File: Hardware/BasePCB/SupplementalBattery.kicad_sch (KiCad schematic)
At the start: 28 parts, among them J1 53307-2471, Q6 IRLML0030

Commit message: only 4 traces left
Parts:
- added J10: 575-4, UTSVT_Connectors:5754, symbol Connector_Generic:Conn_01x01
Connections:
- net SUPP_REG+: now also J10.1 (Pin_1)
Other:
- note added: "24V injector"
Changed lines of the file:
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@@
 		)
 	)
+	(text "24V injector"
+		(exclude_from_sim no)
+		(at 202.184 33.274 0)
+		(effects
+			(font
+				(size 1.27 1.27)
+			)
+		)
+	)
 	(text "Connector to SuppMon Hat"
 		(exclude_from_sim no)
@@
 	)
 	(junction
+		(at 201.93 43.18)
+		(diameter 0)
+		(color 0 0 0 0)
+	)
+	(junction
 		(at 189.23 43.18)
 		(diameter 0)
@@
 	(wire
 		(pts
+			(xy 196.85 34.29) (xy 201.93 34.29)
+		)
+		(stroke
+			(width 0)
+			(type default)
+		)
+	)
+	(wire
+		(pts
 			(xy 34.29 68.58) (xy 34.29 69.85)
 		)
@@
 	(wire
 		(pts
-			(xy 189.23 43.18) (xy 203.2 43.18)
+			(xy 189.23 43.18) (xy 201.93 43.18)
 		)
 		(stroke
@@
 	(wire
 		(pts
+			(xy 201.93 34.29) (xy 201.93 43.18)
+		)
+		(stroke
+			(width 0)
+			(type default)
+		)
+	)
+	(wire
+		(pts
 			(xy 40.64 43.18) (xy 49.53 43.18)
 		)
@@
 	(wire
 		(pts
+			(xy 201.93 43.18) (xy 203.2 43.18)
+		)
+		(stroke
+			(width 0)
+			(type default)
+		)
+	)
+	(wire
+		(pts
 			(xy 83.82 137.16) (xy 88.9 137.16)
 		)
@@
 	)
 	(symbol
+		(lib_id "Connector_Generic:Conn_01x01")
+		(at 191.77 34.29 0)
+		(mirror y)
+		(unit 1)
+		(exclude_from_sim no)
+		(in_bom yes)
+		(on_board yes)
+		(dnp no)
+		(fields_autoplaced yes)
+		(property "Reference" "J10"
+			(at 191.77 27.94 0)
+			(effects
+				(font
+					(size 1.27 1.27)
+				)
+			)
+		)
+		(property "Value" "575-4"
+			(at 191.77 30.48 0)
+			(effects
+				(font
+					(size 1.27 1.27)
+				)
+			)
+		)
+		(property "Footprint" "UTSVT_Connectors:5754"
+			(at 191.77 34.29 0)
+			(effects
+				(font
+					(size 1.27 1.27)
+				)
+				(hide yes)
+			)
+		)
+		(property "Datasheet" "~"
+			(at 191.77 34.29 0)
+			(effects
+				(font
+					(size 1.27 1.27)
+				)
+				(hide yes)
+			)
+		)
+		(property "Description" "Generic connector, single row, 01x01, script generated (kicad-library-utils/schlib/autogen/connector/)"
+			(at 191.77 34.29 0)
+			(effects
+				(font
+					(size 1.27 1.27)
+				)
+				(hide yes)
+			)
+		)
+		(property "P/N" "575-4"
+			(at 191.77 34.29 0)
+			(effects
+				(font
+					(size 1.27 1.27)
+				)
+				(hide yes)
+			)
+		)
+		(property "Mouser P/N" "534-575-4"
+			(at 191.77 34.29 0)
+			(effects
+				(font
+					(size 1.27 1.27)
+				)
+				(hide yes)
+			)
+		)
+		(property "Digikey P/N" "36-575-4-ND"
+			(at 191.77 34.29 0)
+			(effects
+				(font
+					(size 1.27 1.27)
+				)
+				(hide yes)
+			)
+		)
+		(pin "1"
+		)
+		(instances
+			(project "LV Carrier Board"
+				(path "/c5c5922b-1600-4b67-acf3-33264cecd75b/d4cbd764-e723-45ee-b4b7-e620455af31e"
+					(reference "J10")
+					(unit 1)
+				)
+			)
+		)
+	)
+	(symbol
 		(lib_id "Connector:TestPoint")
 		(at 189.23 43.18 0)
@@
 			)
 		)
-		(pin "INP" input
+		(pin "INP" bidirectional
 			(at 107.95 43.18 180)
 			(effects
@@
 			)
 		)
-		(pin "INN" output
+		(pin "INN" bidirectional
 			(at 132.08 43.18 0)
 			(effects

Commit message: add JLC p/n
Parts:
- D14, D15, D16: Assemble (none) -> Y; LSCC P/N (none) -> C7371904
- J1: Assemble (none) -> N; Mouser Price/Stock https://www.mouser.co.uk/ProductDetail/Molex/53307-2471?qs=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 -> (none)
- J10, TP1, TP11, TP12, TP19, TP2, TP21, TP28, TP3, TP7, TP8: Assemble (none) -> N
- Q6: Assemble (none) -> Y; LSCC P/N (none) -> C67272; P/N (none) -> IRLML0030
- R1: Assemble (none) -> Y; LSCC P/N (none) -> C23354
- R14, R15: Assemble (none) -> N; LSCC P/N (none) -> C25804
- R27, R28, R29: Assemble (none) -> Y; LSCC P/N (none) -> C23162
- R30, R34: Assemble (none) -> N; LSCC P/N (none) -> C21189
- R33: Assemble (none) -> Y; LSCC P/N (none) -> C25803; P/N CRCW06034K30FKTA -> CRCW0603100KFKEE
- R41: Assemble (none) -> Y; LSCC P/N (none) -> C21190
- R44: Assemble (none) -> Y; LSCC P/N (none) -> C25804
- U4: Assemble (none) -> N; Datasheet2 https://www.vicorpower.com/documents/datasheets/ds_24vin-mi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 -> (none)

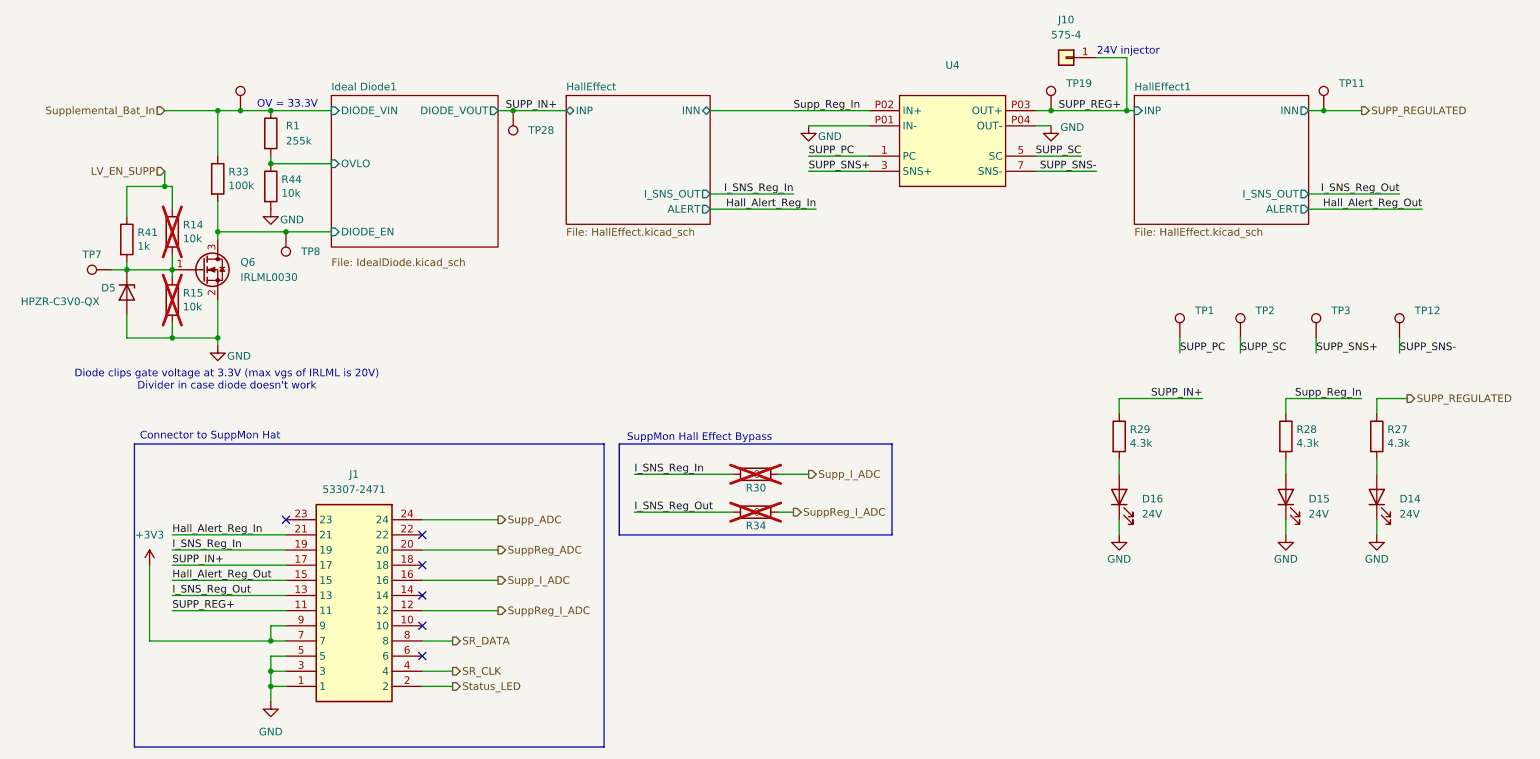
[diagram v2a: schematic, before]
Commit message: new hall effect IC
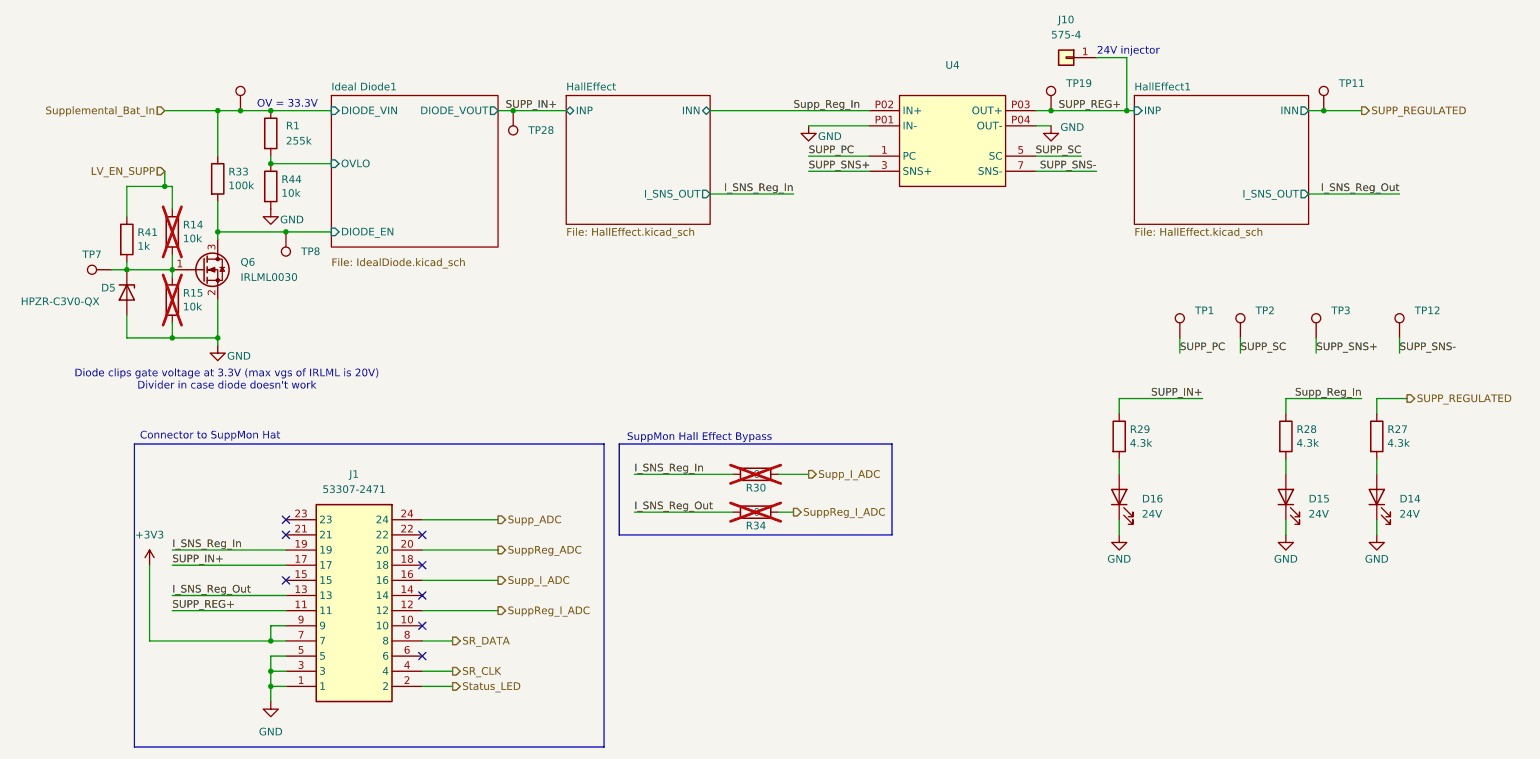
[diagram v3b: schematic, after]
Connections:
- net Hall_Alert_Reg_In: no longer names the net of J1.21
- net Hall_Alert_Reg_Out: no longer names the net of J1.15
- no-connect marks 6 -> 8
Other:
- sheet HallEffect ports: added none; removed ALERT
- sheet HallEffect1 ports: added none; removed ALERT
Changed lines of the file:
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@@
 		(at 60.96 111.76)
 	)
+	(no_connect
+		(at 60.96 114.3)
+	)
+	(no_connect
+		(at 60.96 121.92)
+	)
 	(wire
 		(pts
@@
 	(wire
 		(pts
-			(xy 41.91 121.92) (xy 60.96 121.92)
-		)
-		(stroke
-			(width 0)
-			(type default)
-		)
-	)
-	(wire
-		(pts
 			(xy 31.75 69.85) (xy 34.29 69.85)
 		)
@@
 	(wire
 		(pts
-			(xy 132.08 59.69) (xy 149.86 59.69)
-		)
-		(stroke
-			(width 0)
-			(type default)
-		)
-	)
-	(wire
-		(pts
 			(xy 58.42 129.54) (xy 58.42 132.08)
 		)
@@
 	(wire
 		(pts
-			(xy 41.91 114.3) (xy 60.96 114.3)
-		)
-		(stroke
-			(width 0)
-			(type default)
-		)
-	)
-	(wire
-		(pts
 			(xy 243.84 91.44) (xy 248.92 91.44)
 		)
@@
 	(wire
 		(pts
-			(xy 232.41 59.69) (xy 251.46 59.69)
-		)
-		(stroke
-			(width 0)
-			(type default)
-		)
-	)
-	(wire
-		(pts
 			(xy 58.42 139.7) (xy 60.96 139.7)
 		)
@@
 		)
 	)
-	(label "Hall_Alert_Reg_Out"
-		(at 251.46 59.69 180)
-		(effects
-			(font
-				(size 1.27 1.27)
-			)
-			(justify right bottom)
-		)
-	)
-	(label "Hall_Alert_Reg_In"
-		(at 41.91 114.3 0)
-		(effects
-			(font
-				(size 1.27 1.27)
-			)
-			(justify left bottom)
-		)
-	)
 	(label "SUPP_PC"
 		(at 210.82 83.82 0)
@@
 		)
 	)
-	(label "Hall_Alert_Reg_In"
-		(at 149.86 59.69 180)
-		(effects
-			(font
-				(size 1.27 1.27)
-			)
-			(justify right bottom)
-		)
-	)
 	(label "SUPP_IN+"
 		(at 97.79 43.18 0)
@@
 		)
 	)
-	(label "Hall_Alert_Reg_Out"
-		(at 41.91 121.92 0)
-		(effects
-			(font
-				(size 1.27 1.27)
-			)
-			(justify left bottom)
-		)
-	)
 	(label "I_SNS_Reg_Out"
 		(at 247.65 57.15 180)
@@
 			)
 		)
-		(pin "ALERT" output
-			(at 232.41 59.69 0)
-			(effects
-				(font
-					(size 1.27 1.27)
-				)
-				(justify right)
-			)
-		)
 		(instances
 			(project "LV Carrier Board"
@@
 			(effects
 				(font
-					(size 1.27 1.27)
-				)
-				(justify right)
-			)
-		)
-		(pin "ALERT" output
-			(at 132.08 59.69 0)
-			(effects
-				(font

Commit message: lil shah pt 3
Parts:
- D14, D15, D16: LSCC P/N C7371904 -> (none); LSCS P/N (none) -> C7371904
- Q6: LSCC P/N C67272 -> (none); LSCS P/N (none) -> C67272
- R1: LSCC P/N C23354 -> (none); LSCS P/N (none) -> C23354
- R14, R15, R44: LSCC P/N C25804 -> (none); LSCS P/N (none) -> C25804
- R27, R28, R29: LSCC P/N C23162 -> (none); LSCS P/N (none) -> C23162
- R30, R34: LSCC P/N C21189 -> (none); LSCS P/N (none) -> C21189
- R33: LSCC P/N C25803 -> (none); LSCS P/N (none) -> C25803
- R41: LSCC P/N C21190 -> (none); LSCS P/N (none) -> C21190
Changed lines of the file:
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@@
 			)
 		)
-		(property "LSCC P/N" "C7371904"
+		(property "Assemble" "Y"
 			(at 200.66 107.95 90)
 			(effects
@@
 			)
 		)
-		(property "Assemble" "Y"
+		(property "LSCS P/N" "C7371904"
 			(at 200.66 107.95 90)
 			(effects
@@
 			)
 		)
-		(property "LSCC P/N" ""
-			(at 210.82 81.28 0)
-			(effects
-				(font
-					(size 1.27 1.27)
-				)
-				(hide yes)
-			)
-		)
 		(property "Assemble" "N"
 			(at 210.82 81.28 0)
@@
 			)
 		)
-		(property "LSCC P/N" ""
-			(at 83.82 111.76 0)
-			(effects
-				(font
-					(size 1.27 1.27)
-				)
-				(hide yes)
-			)
-		)
 		(property "Assemble" "N"
 			(at 83.82 111.76 0)
@@
 			)
 		)
-		(property "LSCC P/N" "C25803"
+		(property "Assemble" "Y"
 			(at 49.53 54.61 0)
 			(effects
@@
 			)
 		)
-		(property "Assemble" "Y"
+		(property "LSCS P/N" "C25803"
 			(at 49.53 54.61 0)
 			(effects
@@
 			)
 		)
-		(property "LSCC P/N" ""
-			(at 220.98 81.28 0)
-			(effects
-				(font
-					(size 1.27 1.27)
-				)
-				(hide yes)
-			)
-		)
 		(property "Assemble" "N"
 			(at 220.98 81.28 0)
@@
 			)
 		)
-		(property "LSCC P/N" ""
-			(at 34.29 73.66 90)
-			(effects
-				(font
-					(size 1.27 1.27)
-				)
-				(hide yes)
-			)
-		)
 		(property "Assemble" ""
 			(at 34.29 73.66 90)
@@
 			)
 		)
-		(property "LSCC P/N" ""
-			(at 53.34 43.18 0)
-			(effects
-				(font
-					(size 1.27 1.27)
-				)
-				(hide yes)
-			)
-		)
 		(property "Assemble" "N"
 			(at 53.34 43.18 0)
@@
 			)
 		)
-		(property "LSCC P/N" "C23162"
+		(property "Assemble" "Y"
 			(at 200.66 97.79 0)
 			(effects
@@
 			)
 		)
-		(property "Assemble" "Y"
+		(property "LSCS P/N" "C23162"
 			(at 200.66 97.79 0)
 			(effects
@@
 			)
 		)
-		(property "LSCC P/N" ""
-			(at 233.68 81.28 0)
-			(effects
-				(font
-					(size 1.27 1.27)
-				)
-				(hide yes)
-			)
-		)
 		(property "Assemble" "N"
 			(at 233.68 81.28 0)
@@
 			)
 		)
-		(property "LSCC P/N" "C25804"
+		(property "Assemble" "N"
 			(at 41.91 63.5 0)
 			(effects
@@
 			)
 		)
-		(property "Assemble" "N"
+		(property "LSCS P/N" "C25804"
 			(at 41.91 63.5 0)
 			(effects
@@
 			)
 		)
-		(property "LSCC P/N" "C25804"
+		(property "Assemble" "Y"
 			(at 58.42 55.88 0)
 			(effects
@@
 			)
 		)
-		(property "Assemble" "Y"
+		(property "LSCS P/N" "C25804"
 			(at 58.42 55.88 0)
 			(effects
@@
 			)
 		)
-		(property "LSCC P/N" ""
-			(at 99.06 43.18 0)
-			(effects
-				(font
-					(size 1.27 1.27)
-				)
-				(hide yes)
-			)
-		)
 		(property "Assemble" "N"
 			(at 99.06 43.18 0)
@@
 			)
 		)
-		(property "LSCC P/N" "C7371904"
+		(property "Assemble" "Y"
 			(at 243.84 107.95 90)
 			(effects
@@
 			)
 		)
-		(property "Assemble" "Y"
+		(property "LSCS P/N" "C7371904"
 			(at 243.84 107.95 90)
 			(effects
@@
 			)
 		)
-		(property "LSCC P/N" "C23162"
+		(property "Assemble" "Y"
 			(at 228.6 97.79 0)
 			(effects
@@
 			)
 		)
-		(property "Assemble" "Y"
+		(property "LSCS P/N" "C23162"
 			(at 228.6 97.79 0)
 			(effects
@@
 			)
 		)
-		(property "LSCC P/N" "C7371904"
+		(property "Assemble" "Y"
 			(at 228.6 107.95 90)
 			(effects
@@
 			)
 		)
-		(property "Assemble" "Y"
+		(property "LSCS P/N" "C7371904"
 			(at 228.6 107.95 90)
 			(effects
@@
 			)
 		)
-		(property "LSCC P/N" "C25804"
+		(property "Assemble" "N"
 			(at 41.91 74.93 0)
 			(effects
@@
 			)
 		)
-		(property "Assemble" "N"
+		(property "LSCS P/N" "C25804"
 			(at 41.91 74.93 0)
 			(effects
@@
 			)
 		)
-		(property "LSCC P/N" "C23354"
+		(property "Assemble" "Y"
 			(at 58.42 46.99 0)
 			(effects
@@
 			)
 		)
-		(property "Assemble" "Y"
+		(property "LSCS P/N" "C23354"
 			(at 58.42 46.99 0)
 			(effects
@@
 			)
 		)
-		(property "LSCC P/N" "C23162"
+		(property "Assemble" "Y"
 			(at 243.84 97.79 0)
 			(effects
@@
 			)
 		)
-		(property "Assemble" "Y"
+		(property "LSCS P/N" "C23162"
 			(at 243.84 97.79 0)
 			(effects
@@
 			)
 		)
-		(property "LSCC P/N" ""
-			(at 31.75 69.85 90)
-			(effects
-				(font
-					(size 1.27 1.27)
-				)
-				(hide yes)
-			)
-		)
 		(property "Assemble" "N"
 			(at 31.75 69.85 90)
@@
 			)
 		)
-		(property "LSCC P/N" ""
-			(at 172.72 38.1 0)
-			(effects
-				(font
-					(size 1.27 1.27)
-				)
-				(hide yes)
-			)
-		)
 		(property "Assemble" "N"
 			(at 172.72 38.1 0)
@@
 			)
 		)
-		(property "LSCC P/N" "C21189"
+		(property "Assemble" "N"
 			(at 139.7 110.49 90)
 			(effects
@@
 			)
 		)
-		(property "Assemble" "N"
+		(property "LSCS P/N" "C21189"
 			(at 139.7 110.49 90)
 			(effects
@@
 			)
 		)
-		(property "LSCC P/N" ""
-			(at 191.77 34.29 0)
-			(effects
-				(font
-					(size 1.27 1.27)
-				)
-				(hide yes)
-			)
-		)
 		(property "Assemble" "N"
 			(at 191.77 34.29 0)
@@
 			)
 		)
-		(property "LSCC P/N" ""
-			(at 189.23 43.18 0)
-			(effects
-				(font
-					(size 1.27 1.27)
-				)
-				(hide yes)
-			)
-		)
 		(property "Assemble" "N"
 			(at 189.23 43.18 0)
@@
 			)
 		)
-		(property "LSCC P/N" "C21190"
+		(property "Assemble" "Y"
 			(at 34.29 64.77 0)
 			(effects
@@
 			)
 		)
-		(property "Assemble" "Y"
+		(property "LSCS P/N" "C21190"
 			(at 34.29 64.77 0)
 			(effects
@@
 			)
 		)
-		(property "LSCC P/N" ""
-			(at 247.65 81.28 0)
-			(effects
-				(font
-					(size 1.27 1.27)
-				)
-				(hide yes)
-			)
-		)
 		(property "Assemble" "N"
 			(at 247.65 81.28 0)
@@
 			)
 		)
-		(property "LSCC P/N" "C21189"
+		(property "Assemble" "N"
 			(at 139.7 104.14 90)
 			(effects
@@
 			)
 		)
-		(property "Assemble" "N"
+		(property "LSCS P/N" "C21189"
 			(at 139.7 104.14 90)
 			(effects
@@
 			)
 		)
-		(property "LSCC P/N" "C67272"
+		(property "P/N" "IRLML0030"
 			(at 46.99 69.85 0)
 			(effects
@@
 			)
 		)
-		(property "P/N" "IRLML0030"
+		(property "Assemble" "Y"
 			(at 46.99 69.85 0)
 			(effects
@@
 			)
 		)
-		(property "Assemble" "Y"
+		(property "LSCS P/N" "C67272"
 			(at 46.99 69.85 0)
 			(effects
@@
 			)
 		)
-		(property "LSCC P/N" ""
-			(at 234.95 43.18 0)
-			(effects
-				(font
-					(size 1.27 1.27)
-				)
-				(hide yes)
-			)
-		)
 		(property "Assemble" "N"
 			(at 234.95 43.18 0)
@@
 			(at 60.96 63.5 0)
 			(effects
-				(font
-					(size 1.27 1.27)
-				)
-				(hide yes)
-			)
-		)
-		(property "LSCC P/N" ""
-			(at 60.96 63.5 0)
-			(effects

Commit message: lil shah pt 3.5
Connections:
- net SuppReg_ADC renamed SuppReg_V_ADC
- net Supp_ADC renamed Supp_V_ADC
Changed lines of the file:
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@@
 		)
 	)
-	(hierarchical_label "Supp_ADC"
+	(hierarchical_label "Supp_V_ADC"
 		(shape output)
 		(at 96.52 111.76 0)
@@
 		)
 	)
-	(hierarchical_label "SuppReg_ADC"
+	(hierarchical_label "SuppReg_V_ADC"
 		(shape output)
 		(at 96.52 116.84 0)

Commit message: balls
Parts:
- removed J10: 575-4, UTSVT_Connectors:5754, symbol Connector_Generic:Conn_01x01
- removed R30, R34: 0, Resistor_SMD:R_0603_1608Metric_Pad0.98x0.95mm_HandSolder, symbol Device:R
- added R17, R20: 10k, Resistor_SMD:R_0603_1608Metric_Pad0.98x0.95mm_HandSolder, symbol Device:R
- added R2, R46: 1k, Resistor_SMD:R_0603_1608Metric_Pad0.98x0.95mm_HandSolder, symbol Device:R
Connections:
- net GND: now also R2.2, R46.2
- net SUPP_IN+: now also R20.1
- net SuppReg_V_ADC: now also R17.2, R2.1
- net Supp_Reg_In: now also R17.1
- net Supp_V_ADC: now also R20.2, R46.1
- net I_SNS_Reg_In: no longer names the net of J1.19
- net I_SNS_Reg_Out: no longer names the net of J1.13
- no-connect marks 8 -> 10
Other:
- note removed: "24V injector"
- note removed: "SuppMon Hall Effect Bypass"
- moved on the sheet: D16, R29, TP28

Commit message: balls
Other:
- note added: "Divider of 11 Max Supp Voltage = 30V, divided = 2.72V Min supp Voltage = 18V, divided = 1.63V"
- note added: "Divider of 11 Max SuppReg Voltage = 25, divided = 2.27V Min supp Voltage = 23.9, divided = 2.27V"
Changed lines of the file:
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@@
 	(paper "A4")
 	(rectangle
-		(start 24.13 99.06)
+		(start 24.13 102.87)
 		(end 114.3 149.86)
 		(stroke
@@
 	(text "Connector to SuppMon Hat"
 		(exclude_from_sim no)
-		(at 48.26 97.79 0)
+		(at 36.83 101.6 0)
 		(effects
 			(font
 				(size 1.27 1.27)
 			)
+		)
+	)
+	(text "Divider of 11\nMax Supp Voltage = 30V, divided = 2.72V\nMin supp Voltage = 18V, divided = 1.63V\n"
+		(exclude_from_sim no)
+		(at 108.966 97.282 0)
+		(effects
+			(font
+				(size 1.27 1.27)
+			)
+			(justify left)
 		)
 	)
@@
 		)
 	)
+	(text "Divider of 11\nMax SuppReg Voltage = 25, divided = 2.27V\nMin supp Voltage = 23.9, divided = 2.27V\n"
+		(exclude_from_sim no)
+		(at 155.448 97.028 0)
+		(effects
+			(font
+				(size 1.27 1.27)
+			)
+			(justify left)
+		)
+	)

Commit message: updated p/n
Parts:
- removed R17, R20: 10k, Resistor_SMD:R_0603_1608Metric_Pad0.98x0.95mm_HandSolder, symbol Device:R
- removed R2, R46: 1k, Resistor_SMD:R_0603_1608Metric_Pad0.98x0.95mm_HandSolder, symbol Device:R
- added J10: 575-4, UTSVT_Connectors:5754, symbol Connector_Generic:Conn_01x01
- added R30, R34: 0, Resistor_SMD:R_0603_1608Metric_Pad0.98x0.95mm_HandSolder, symbol Device:R
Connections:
- net SUPP_REG+: now also J10.1 (Pin_1)
- net SuppReg_I_ADC: now also R34.2
- net Supp_I_ADC: now also R30.2
- net I_SNS_Reg_Out: now reaches J1.13
- net I_SNS_Reg_Out: now also R34.1
- net I_SNS_Reg_In: now reaches J1.19
- net I_SNS_Reg_In: now also R30.1
- no-connect marks 10 -> 8
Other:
- note added: "24V injector"
- note added: "SuppMon Hall Effect Bypass"
- note removed: "Divider of 11 Max Supp Voltage = 30V, divided = 2.72V Min supp Voltage = 18V, divided = 1.63V"
- note removed: "Divider of 11 Max SuppReg Voltage = 25, divided = 2.27V Min supp Voltage = 23.9, divided = 2.27V"
- moved on the sheet: D16, R29, TP28
